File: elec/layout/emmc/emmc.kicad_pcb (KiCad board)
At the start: 2 copper layers, 40 x 40 mm, 10 parts, among them U1 _Samsung_KLMBG2JETD_B041

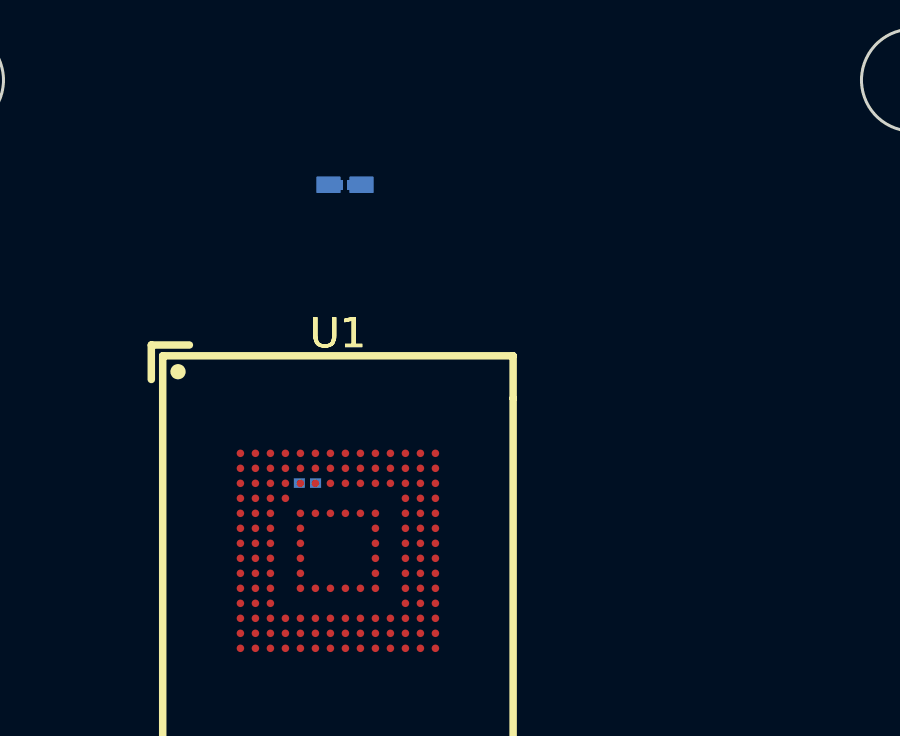
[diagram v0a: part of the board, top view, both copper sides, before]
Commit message: Manual net naming
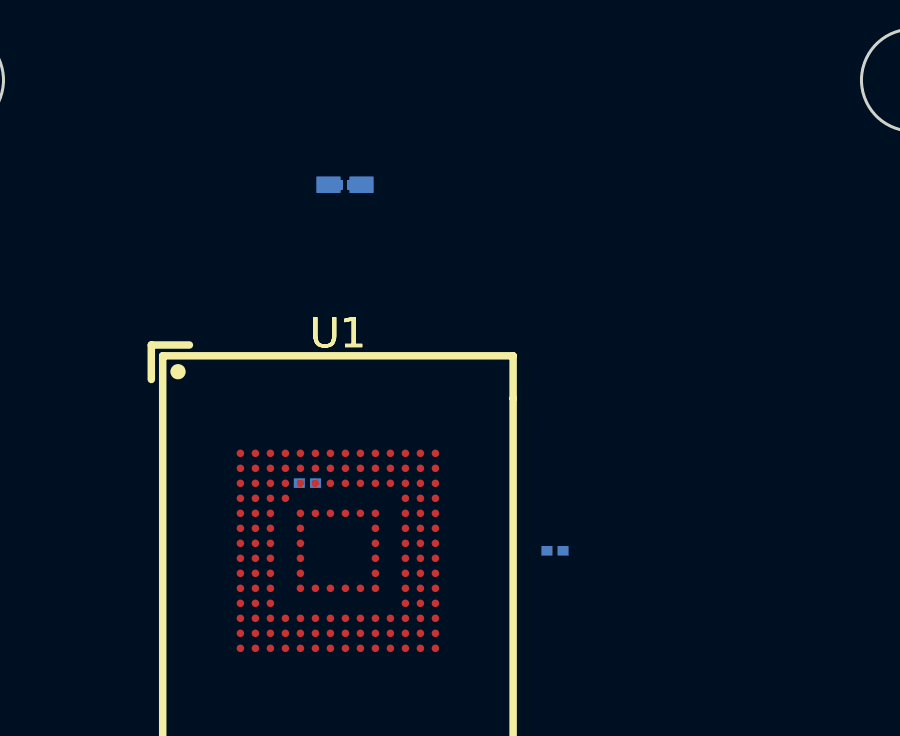
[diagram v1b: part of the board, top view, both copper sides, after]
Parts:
- moved C4 14.1 mm to (153.4, 97.8)
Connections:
- net *7ED8.eMMC-net-0 renamed VDD_1V8
- net *7ED8.eMMC-net-1 renamed VDD_3V3
- net *7ED8.eMMC-signal-0 renamed eMMC_CMD
- net *7ED8.eMMC-signal-1 renamed eMMC_CLK
- net *7ED8.eMMC-signal-2 renamed eMMC_DATA_STROBE
- net *7ED8.eMMC-signal-3 renamed eMMC_RSTN
- net *7ED8.eMMC.eMMC-net-0 renamed net
- net *7ED8.eMMC.eMMC-net-2 renamed VDD_INTERNAL
- net signal-0 renamed eMMC_DAT_2
- net signal-1 renamed eMMC_DAT_0
- net signal-2 renamed eMMC_DAT_7
- net signal-3 renamed eMMC_DAT_1
- net signal-4 renamed eMMC_DAT_6
- net signal-5 renamed eMMC_DAT_5
- net signal-6 renamed eMMC_DAT_3
- net signal-7 renamed eMMC_DAT_4
- C1 pad 2: lv -> GND
- C2 pad 2: lv -> GND
- C3 pad 2: lv -> GND
- C4 pad 2: lv -> GND
- C5 pad 2: lv -> GND
- C6 pad 2: lv -> GND
- C7 pad 2: lv -> GND
- C8 pad 2: lv -> GND
- C9 pad 2: lv -> GND
- U1 pad A6: *7ED8.eMMC.eMMC-net-1 -> GND
- U1 pad C4: *7ED8.eMMC.eMMC-net-1 -> GND
- U1 pad E7: *7ED8.eMMC.eMMC-net-1 -> GND
- U1 pad G5: *7ED8.eMMC.eMMC-net-1 -> GND
- U1 pad H10: *7ED8.eMMC.eMMC-net-1 -> GND
- U1 pad J5: *7ED8.eMMC.eMMC-net-1 -> GND
- U1 pad K8: *7ED8.eMMC.eMMC-net-1 -> GND
- U1 pad N2: *7ED8.eMMC.eMMC-net-1 -> GND
- U1 pad N5: *7ED8.eMMC.eMMC-net-1 -> GND
- U1 pad P4: *7ED8.eMMC.eMMC-net-1 -> GND
- U1 pad P6: *7ED8.eMMC.eMMC-net-1 -> GND

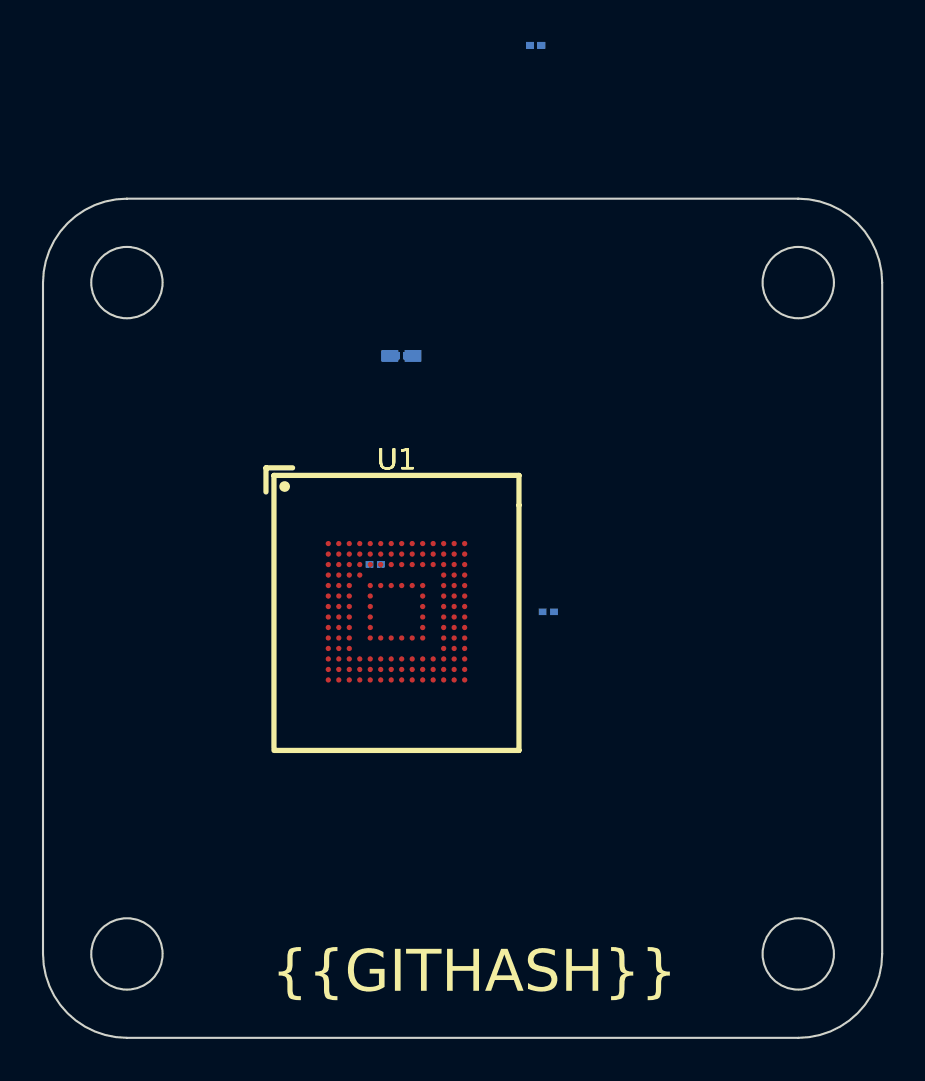
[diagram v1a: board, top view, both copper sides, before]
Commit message: add extra decoupling caps to 3v3 rail + update layout
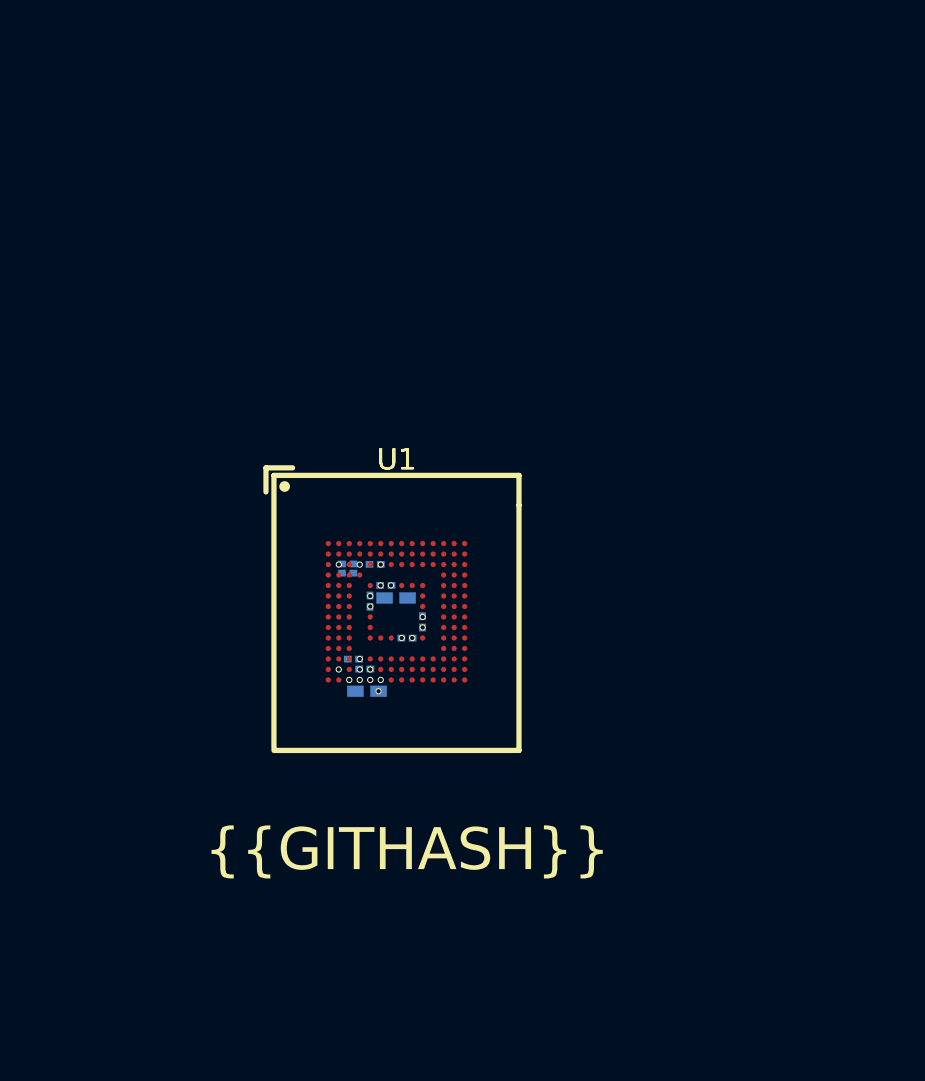
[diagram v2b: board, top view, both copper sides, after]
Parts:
- added C10: 220nF ±20% 6.3V X5R, lcsc:C0201, B.Cu at (147.4, 98.3)
- added C11: 220nF ±20% 6.3V X5R, lcsc:C0201, B.Cu at (146.7, 99.1)
- moved C8 26.7 mm to (143.9, 96.0), turned to 0 degrees
- moved C9 26.3 mm to (143.9, 95.5), turned to 0 degrees
- moved C1 16.1 mm to (144.8, 101.6), turned to 0 degrees
- moved C3 15.0 mm to (144.7, 100.5), turned to 0 degrees
- moved C7 11.8 mm to (144.9, 97.3), turned to -90 degrees
- moved C5 11.5 mm to (146.2, 97.1), turned to 0 degrees
- moved C6 11.0 mm to (145.7, 96.5), turned to 0 degrees
- moved C4 9.56 mm to (144.1, 100.1)
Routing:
- net VDD_INTERNAL: vias 0 -> 1
- net VDD_3V3: vias 0 -> 4
- net VDD_1V8: vias 0 -> 5
- net GND: vias 0 -> 10
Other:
- board outline removed

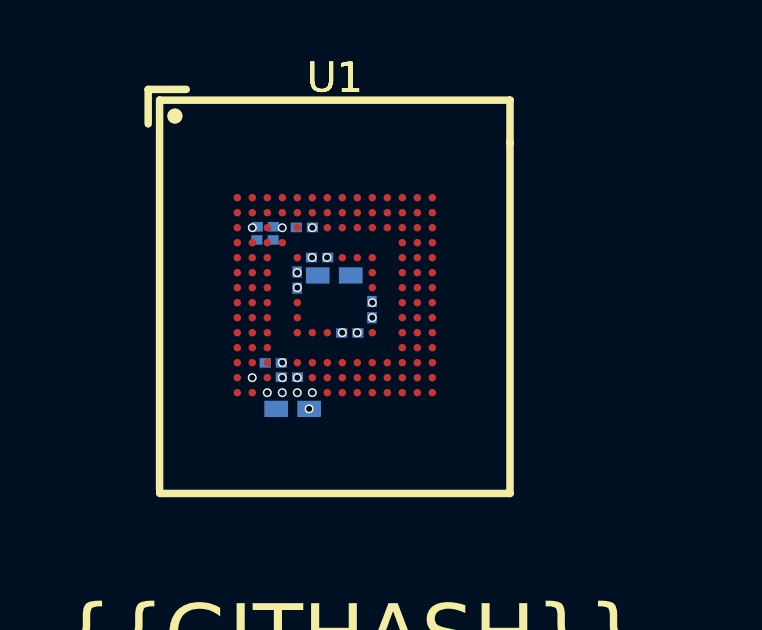
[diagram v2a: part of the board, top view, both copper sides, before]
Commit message: Update decoupling caps to use for loops and multiple decoupling caps and update layout
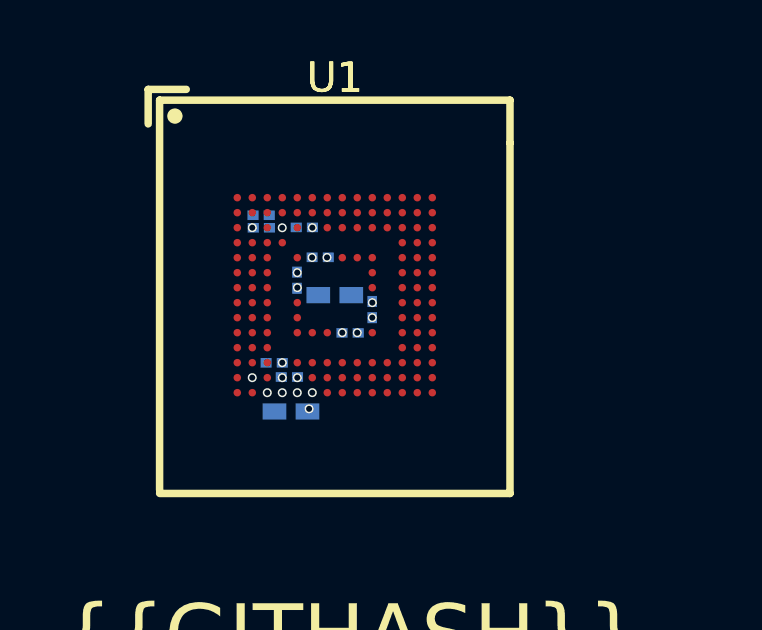
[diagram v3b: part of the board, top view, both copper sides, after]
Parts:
- C10: value 220nF ±20% 6.3V X5R -> 1µF ±20% 6.3V X5R
- C8: value 1µF ±20% 6.3V X5R -> 220nF ±20% 6.3V X5R
- moved C11 4.91 mm to (143.7, 95.1), turned to 0 degrees
- moved C10 4.59 mm to (143.8, 95.6), turned to 0 degrees
- moved C9 4.50 mm to (147.4, 98.3), turned to 90 degrees
- moved C8 4.20 mm to (146.7, 99.1), turned to 180 degrees
- moved C5 0.66 mm to (146.2, 97.8)
- moved C1 0.10 mm to (144.7, 101.7)
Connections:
- net net renamed *3DB8.eMMC-net
- C10 pad 1: VDD_3V3 -> VDD_INTERNAL
- C10 pad 2: GND -> *3DB8.eMMC.VDD_INTERNAL-net
- C11 pad 1: VDD_3V3 -> VDD_INTERNAL
- C11 pad 2: GND -> *3DB8.eMMC.VDD_INTERNAL-net
- C8 pad 1: VDD_INTERNAL -> VDD_3V3
- C9 pad 1: VDD_INTERNAL -> VDD_3V3

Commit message: Update ato.yaml to build nonos + import into layout
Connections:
- net *3DB8.eMMC.VDD_INTERNAL-net renamed *2E88.eMMC.VDD_INTERNAL-net
- net GND renamed lv
- net VDD_1V8 renamed hv
- net VDD_3V3 renamed *2E88-net
- U1 pad A1: *3DB8.eMMC-net -> *2E88.eMMC.footprint.pins[0].net-net
- U1 pad A10: *3DB8.eMMC-net -> *2E88.eMMC.footprint.pins[1].net-net
- U1 pad A11: *3DB8.eMMC-net -> *2E88.eMMC.footprint.pins[2].net-net
- U1 pad A12: *3DB8.eMMC-net -> *2E88.eMMC.footprint.pins[3].net-net
- U1 pad A13: *3DB8.eMMC-net -> *2E88.eMMC.footprint.pins[4].net-net
- U1 pad A14: *3DB8.eMMC-net -> *2E88.eMMC.footprint.pins[5].net-net
- U1 pad A2: *3DB8.eMMC-net -> *2E88.eMMC.footprint.pins[6].net-net
- U1 pad A7: *3DB8.eMMC-net -> *2E88.eMMC.footprint.pins[11].net-net
- U1 pad A8: *3DB8.eMMC-net -> *2E88.eMMC.footprint.pins[12].net-net
- U1 pad A9: *3DB8.eMMC-net -> *2E88.eMMC.footprint.pins[13].net-net
- U1 pad B1: *3DB8.eMMC-net -> *2E88.eMMC.footprint.pins[14].net-net
- U1 pad B10: *3DB8.eMMC-net -> *2E88.eMMC.footprint.pins[15].net-net
- U1 pad B11: *3DB8.eMMC-net -> *2E88.eMMC.footprint.pins[16].net-net
- U1 pad B12: *3DB8.eMMC-net -> *2E88.eMMC.footprint.pins[17].net-net
- U1 pad B13: *3DB8.eMMC-net -> *2E88.eMMC.footprint.pins[18].net-net
- U1 pad B14: *3DB8.eMMC-net -> *2E88.eMMC.footprint.pins[19].net-net
- U1 pad B7: *3DB8.eMMC-net -> *2E88.eMMC.footprint.pins[25].net-net
- U1 pad B8: *3DB8.eMMC-net -> *2E88.eMMC.footprint.pins[26].net-net
- U1 pad B9: *3DB8.eMMC-net -> *2E88.eMMC.footprint.pins[27].net-net
- U1 pad C1: *3DB8.eMMC-net -> *2E88.eMMC.footprint.pins[28].net-net
- U1 pad C10: *3DB8.eMMC-net -> *2E88.eMMC.footprint.pins[29].net-net
- U1 pad C11: *3DB8.eMMC-net -> *2E88.eMMC.footprint.pins[30].net-net
- U1 pad C12: *3DB8.eMMC-net -> *2E88.eMMC.footprint.pins[31].net-net
- U1 pad C13: *3DB8.eMMC-net -> *2E88.eMMC.footprint.pins[32].net-net
- U1 pad C14: *3DB8.eMMC-net -> *2E88.eMMC.footprint.pins[33].net-net
- U1 pad C3: *3DB8.eMMC-net -> *2E88.eMMC.footprint.pins[35].net-net
- U1 pad C5: *3DB8.eMMC-net -> *2E88.eMMC.footprint.pins[37].net-net
- U1 pad C7: *3DB8.eMMC-net -> *2E88.eMMC.footprint.pins[39].net-net
- U1 pad C8: *3DB8.eMMC-net -> *2E88.eMMC.footprint.pins[40].net-net
- U1 pad C9: *3DB8.eMMC-net -> *2E88.eMMC.footprint.pins[41].net-net
- U1 pad D1: *3DB8.eMMC-net -> *2E88.eMMC.footprint.pins[42].net-net
- U1 pad D12: *3DB8.eMMC-net -> *2E88.eMMC.footprint.pins[43].net-net
- U1 pad D13: *3DB8.eMMC-net -> *2E88.eMMC.footprint.pins[44].net-net
- U1 pad D14: *3DB8.eMMC-net -> *2E88.eMMC.footprint.pins[45].net-net
- U1 pad D2: *3DB8.eMMC-net -> *2E88.eMMC.footprint.pins[46].net-net
- U1 pad D3: *3DB8.eMMC-net -> *2E88.eMMC.footprint.pins[47].net-net
- U1 pad D4: *3DB8.eMMC-net -> *2E88.eMMC.footprint.pins[48].net-net
- U1 pad E1: *3DB8.eMMC-net -> *2E88.eMMC.footprint.pins[49].net-net
- U1 pad E10: *3DB8.eMMC-net -> *2E88.eMMC.footprint.pins[50].net-net
- U1 pad E12: *3DB8.eMMC-net -> *2E88.eMMC.footprint.pins[51].net-net
- U1 pad E13: *3DB8.eMMC-net -> *2E88.eMMC.footprint.pins[52].net-net
- U1 pad E14: *3DB8.eMMC-net -> *2E88.eMMC.footprint.pins[53].net-net
- U1 pad E2: *3DB8.eMMC-net -> *2E88.eMMC.footprint.pins[54].net-net
- U1 pad E3: *3DB8.eMMC-net -> *2E88.eMMC.footprint.pins[55].net-net
- U1 pad E5: *3DB8.eMMC-net -> *2E88.eMMC.footprint.pins[56].net-net
- U1 pad E8: *3DB8.eMMC-net -> *2E88.eMMC.footprint.pins[59].net-net
- U1 pad E9: *3DB8.eMMC-net -> *2E88.eMMC.footprint.pins[60].net-net
- U1 pad F1: *3DB8.eMMC-net -> *2E88.eMMC.footprint.pins[61].net-net
- U1 pad F10: *3DB8.eMMC-net -> *2E88.eMMC.footprint.pins[62].net-net
- U1 pad F12: *3DB8.eMMC-net -> *2E88.eMMC.footprint.pins[63].net-net
- U1 pad F13: *3DB8.eMMC-net -> *2E88.eMMC.footprint.pins[64].net-net
- U1 pad F14: *3DB8.eMMC-net -> *2E88.eMMC.footprint.pins[65].net-net
- U1 pad F2: *3DB8.eMMC-net -> *2E88.eMMC.footprint.pins[66].net-net
- U1 pad F3: *3DB8.eMMC-net -> *2E88.eMMC.footprint.pins[67].net-net
- U1 pad G1: *3DB8.eMMC-net -> *2E88.eMMC.footprint.pins[69].net-net
- U1 pad G10: *3DB8.eMMC-net -> *2E88.eMMC.footprint.pins[70].net-net
- U1 pad G12: *3DB8.eMMC-net -> *2E88.eMMC.footprint.pins[71].net-net
- U1 pad G13: *3DB8.eMMC-net -> *2E88.eMMC.footprint.pins[72].net-net
- U1 pad G14: *3DB8.eMMC-net -> *2E88.eMMC.footprint.pins[73].net-net
- U1 pad G2: *3DB8.eMMC-net -> *2E88.eMMC.footprint.pins[74].net-net
- U1 pad G3: *3DB8.eMMC-net -> *2E88.eMMC.footprint.pins[75].net-net
- U1 pad H1: *3DB8.eMMC-net -> *2E88.eMMC.footprint.pins[77].net-net
- U1 pad H12: *3DB8.eMMC-net -> *2E88.eMMC.footprint.pins[79].net-net
- U1 pad H13: *3DB8.eMMC-net -> *2E88.eMMC.footprint.pins[80].net-net
- U1 pad H14: *3DB8.eMMC-net -> *2E88.eMMC.footprint.pins[81].net-net
- U1 pad H2: *3DB8.eMMC-net -> *2E88.eMMC.footprint.pins[82].net-net
- U1 pad H3: *3DB8.eMMC-net -> *2E88.eMMC.footprint.pins[83].net-net
- U1 pad J1: *3DB8.eMMC-net -> *2E88.eMMC.footprint.pins[85].net-net
- U1 pad J12: *3DB8.eMMC-net -> *2E88.eMMC.footprint.pins[87].net-net
- U1 pad J13: *3DB8.eMMC-net -> *2E88.eMMC.footprint.pins[88].net-net
- U1 pad J14: *3DB8.eMMC-net -> *2E88.eMMC.footprint.pins[89].net-net
- U1 pad J2: *3DB8.eMMC-net -> *2E88.eMMC.footprint.pins[90].net-net
- U1 pad J3: *3DB8.eMMC-net -> *2E88.eMMC.footprint.pins[91].net-net
- U1 pad K1: *3DB8.eMMC-net -> *2E88.eMMC.footprint.pins[93].net-net
- U1 pad K10: *3DB8.eMMC-net -> *2E88.eMMC.footprint.pins[94].net-net
- U1 pad K12: *3DB8.eMMC-net -> *2E88.eMMC.footprint.pins[95].net-net
- U1 pad K13: *3DB8.eMMC-net -> *2E88.eMMC.footprint.pins[96].net-net
- U1 pad K14: *3DB8.eMMC-net -> *2E88.eMMC.footprint.pins[97].net-net
- U1 pad K2: *3DB8.eMMC-net -> *2E88.eMMC.footprint.pins[98].net-net
- U1 pad K3: *3DB8.eMMC-net -> *2E88.eMMC.footprint.pins[99].net-net
- U1 pad K6: *3DB8.eMMC-net -> *2E88.eMMC.footprint.pins[101].net-net
- U1 pad K7: *3DB8.eMMC-net -> *2E88.eMMC.footprint.pins[102].net-net
- U1 pad L1: *3DB8.eMMC-net -> *2E88.eMMC.footprint.pins[105].net-net
- U1 pad L12: *3DB8.eMMC-net -> *2E88.eMMC.footprint.pins[106].net-net
- U1 pad L13: *3DB8.eMMC-net -> *2E88.eMMC.footprint.pins[107].net-net
- U1 pad L14: *3DB8.eMMC-net -> *2E88.eMMC.footprint.pins[108].net-net
- U1 pad L2: *3DB8.eMMC-net -> *2E88.eMMC.footprint.pins[109].net-net
- U1 pad L3: *3DB8.eMMC-net -> *2E88.eMMC.footprint.pins[110].net-net
- U1 pad M1: *3DB8.eMMC-net -> *2E88.eMMC.footprint.pins[111].net-net
- U1 pad M10: *3DB8.eMMC-net -> *2E88.eMMC.footprint.pins[112].net-net
- U1 pad M11: *3DB8.eMMC-net -> *2E88.eMMC.footprint.pins[113].net-net
- U1 pad M12: *3DB8.eMMC-net -> *2E88.eMMC.footprint.pins[114].net-net
- U1 pad M13: *3DB8.eMMC-net -> *2E88.eMMC.footprint.pins[115].net-net
- U1 pad M14: *3DB8.eMMC-net -> *2E88.eMMC.footprint.pins[116].net-net
- U1 pad M2: *3DB8.eMMC-net -> *2E88.eMMC.footprint.pins[117].net-net
- U1 pad M3: *3DB8.eMMC-net -> *2E88.eMMC.footprint.pins[118].net-net
- U1 pad M7: *3DB8.eMMC-net -> *2E88.eMMC.footprint.pins[122].net-net
- U1 pad M8: *3DB8.eMMC-net -> *2E88.eMMC.footprint.pins[123].net-net
- U1 pad M9: *3DB8.eMMC-net -> *2E88.eMMC.footprint.pins[124].net-net
- U1 pad N1: *3DB8.eMMC-net -> *2E88.eMMC.footprint.pins[125].net-net
- U1 pad N10: *3DB8.eMMC-net -> *2E88.eMMC.footprint.pins[126].net-net
- U1 pad N11: *3DB8.eMMC-net -> *2E88.eMMC.footprint.pins[127].net-net
- U1 pad N12: *3DB8.eMMC-net -> *2E88.eMMC.footprint.pins[128].net-net
- U1 pad N13: *3DB8.eMMC-net -> *2E88.eMMC.footprint.pins[129].net-net
- U1 pad N14: *3DB8.eMMC-net -> *2E88.eMMC.footprint.pins[130].net-net
- U1 pad N3: *3DB8.eMMC-net -> *2E88.eMMC.footprint.pins[132].net-net
- U1 pad N6: *3DB8.eMMC-net -> *2E88.eMMC.footprint.pins[135].net-net
- U1 pad N7: *3DB8.eMMC-net -> *2E88.eMMC.footprint.pins[136].net-net
- U1 pad N8: *3DB8.eMMC-net -> *2E88.eMMC.footprint.pins[137].net-net
- U1 pad N9: *3DB8.eMMC-net -> *2E88.eMMC.footprint.pins[138].net-net
- U1 pad P1: *3DB8.eMMC-net -> *2E88.eMMC.footprint.pins[139].net-net
- U1 pad P10: *3DB8.eMMC-net -> *2E88.eMMC.footprint.pins[140].net-net
- U1 pad P11: *3DB8.eMMC-net -> *2E88.eMMC.footprint.pins[141].net-net
- U1 pad P12: *3DB8.eMMC-net -> *2E88.eMMC.footprint.pins[142].net-net
- U1 pad P13: *3DB8.eMMC-net -> *2E88.eMMC.footprint.pins[143].net-net
- U1 pad P14: *3DB8.eMMC-net -> *2E88.eMMC.footprint.pins[144].net-net
- U1 pad P2: *3DB8.eMMC-net -> *2E88.eMMC.footprint.pins[145].net-net
- U1 pad P7: *3DB8.eMMC-net -> *2E88.eMMC.footprint.pins[150].net-net
- U1 pad P8: *3DB8.eMMC-net -> *2E88.eMMC.footprint.pins[151].net-net
- U1 pad P9: *3DB8.eMMC-net -> *2E88.eMMC.footprint.pins[152].net-net
